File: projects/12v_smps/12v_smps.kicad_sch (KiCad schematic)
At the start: 7 parts, among them U2 TPSM82902SISR

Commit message: wip
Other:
- moved on the sheet: C1, C2, C4, R18, R19, R20, U2

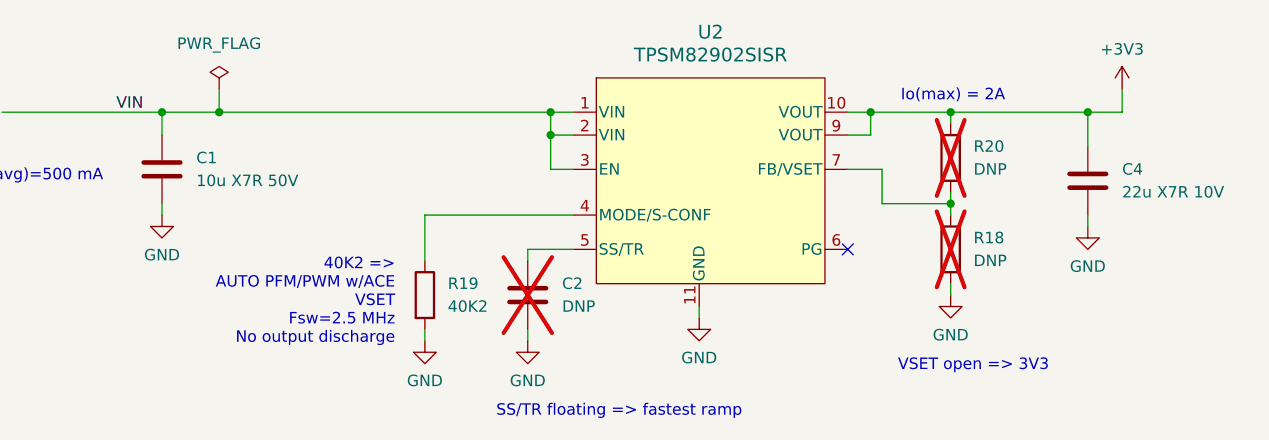
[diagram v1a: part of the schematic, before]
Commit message: 12v smps block
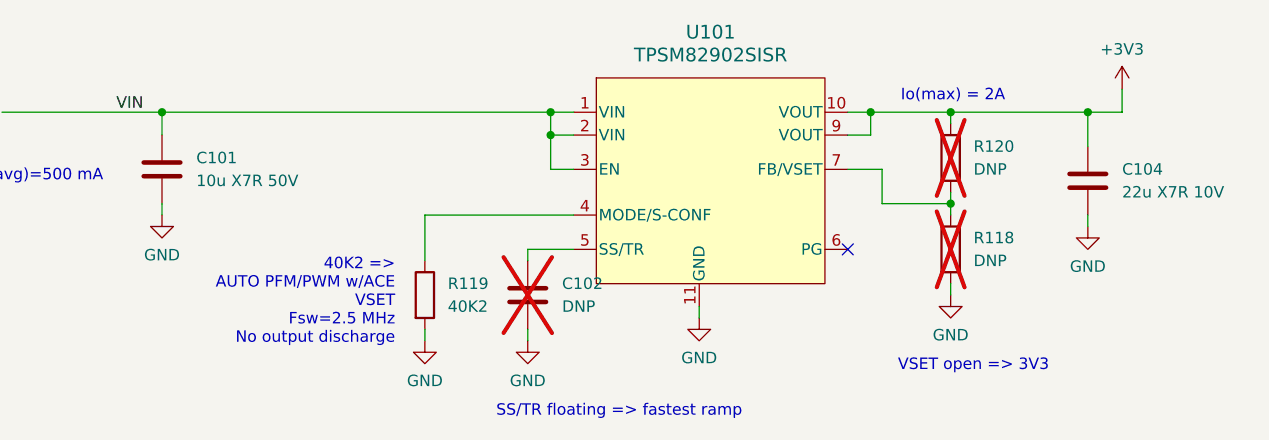
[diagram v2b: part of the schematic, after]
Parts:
- renumbered C1 to C101, C2 to C102, C4 to C104, R18 to R118, R19 to R119, R20 to R120, U2 to U101
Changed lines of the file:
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@@
-	)
-	(junction
-		(at 156.21 88.9)
-		(diameter 0)
-		(color 0 0 0 0)
 	)
 	(junction
@@
 	(wire
 		(pts
-			(xy 156.21 88.9) (xy 193.04 88.9)
+			(xy 149.86 88.9) (xy 193.04 88.9)
 		)
 		(stroke
@@
 	(wire
 		(pts
-			(xy 156.21 86.36) (xy 156.21 88.9)
-		)
-		(stroke
-			(width 0)
-			(type default)
-		)
-	)
-	(wire
-		(pts
 			(xy 149.86 99.06) (xy 149.86 100.33)
 		)
@@
 		(pts
 			(xy 256.54 86.36) (xy 256.54 88.9)
-		)
-		(stroke
-			(width 0)
-			(type default)
-		)
-	)
-	(wire
-		(pts
-			(xy 149.86 88.9) (xy 156.21 88.9)
 		)
 		(stroke
@@
 		(dnp no)
 		(fields_autoplaced yes)
-		(property "Reference" "R19"
+		(property "Reference" "R119"
 			(at 181.61 107.9499 0)
 			(effects
@@
 			(project ""
 				(path "/a5f55489-8083-4ed1-a137-3f799946f30f"
-					(reference "R19")
-					(unit 1)
-				)
-			)
-		)
-	)
-	(symbol
-		(lib_id "power:PWR_FLAG")
-		(at 156.21 86.36 0)
-		(unit 1)
-		(exclude_from_sim no)
-		(in_bom yes)
-		(on_board yes)
-		(dnp no)
-		(fields_autoplaced yes)
-		(property "Reference" "#FLG03"
-			(at 156.21 84.455 0)
-			(effects
-				(font
-					(size 1.27 1.27)
-				)
-				(hide yes)
-			)
-		)
-		(property "Value" "PWR_FLAG"
-			(at 156.21 81.28 0)
-			(effects
-				(font
-					(size 1.27 1.27)
-				)
-			)
-		)
-		(property "Footprint" ""
-			(at 156.21 86.36 0)
-			(effects
-				(font
-					(size 1.27 1.27)
-				)
-				(hide yes)
-			)
-		)
-		(property "Datasheet" "~"
-			(at 156.21 86.36 0)
-			(effects
-				(font
-					(size 1.27 1.27)
-				)
-				(hide yes)
-			)
-		)
-		(property "Description" "Special symbol for telling ERC where power comes from"
-			(at 156.21 86.36 0)
-			(effects
-				(font
-					(size 1.27 1.27)
-				)
-				(hide yes)
-			)
-		)
-		(pin "1"
-		)
-		(instances
-			(project ""
-				(path "/a5f55489-8083-4ed1-a137-3f799946f30f"
-					(reference "#FLG03")
+					(reference "R119")
 					(unit 1)
 				)
@@
 		(dnp no)
 		(fields_autoplaced yes)
-		(property "Reference" "U2"
+		(property "Reference" "U101"
 			(at 210.82 80.01 0)
 			(effects
@@
 			(project ""
 				(path "/a5f55489-8083-4ed1-a137-3f799946f30f"
-					(reference "U2")
+					(reference "U101")
 					(unit 1)
 				)
@@
 		(dnp yes)
 		(fields_autoplaced yes)
-		(property "Reference" "C2"
+		(property "Reference" "C102"
 			(at 194.31 107.9499 0)
 			(effects
@@
 			(project ""
 				(path "/a5f55489-8083-4ed1-a137-3f799946f30f"
-					(reference "C2")
+					(reference "C102")
 					(unit 1)
 				)
@@
 		(dnp yes)
 		(fields_autoplaced yes)
-		(property "Reference" "R18"
+		(property "Reference" "R118"
 			(at 240.03 102.8699 0)
 			(effects
@@
 			(project ""
 				(path "/a5f55489-8083-4ed1-a137-3f799946f30f"
-					(reference "R18")
+					(reference "R118")
 					(unit 1)
 				)
@@
 		(dnp no)
 		(fields_autoplaced yes)
-		(property "Reference" "C4"
+		(property "Reference" "C104"
 			(at 256.54 95.2499 0)
 			(effects
@@
 			(project "canob"
 				(path "/a5f55489-8083-4ed1-a137-3f799946f30f"
-					(reference "C4")
+					(reference "C104")
 					(unit 1)
 				)
@@
 		(dnp no)
 		(fields_autoplaced yes)
-		(property "Reference" "C1"
+		(property "Reference" "C101"
 			(at 153.67 93.9799 0)
 			(effects
@@
 			(project ""
 				(path "/a5f55489-8083-4ed1-a137-3f799946f30f"
-					(reference "C1")
+					(reference "C101")
 					(unit 1)
 				)
@@
 		(dnp yes)
 		(fields_autoplaced yes)
-		(property "Reference" "R20"
+		(property "Reference" "R120"
 			(at 240.03 92.7099 0)
 			(effects
@@
 			(project "canob"
 				(path "/a5f55489-8083-4ed1-a137-3f799946f30f"
-					(reference "R20")
-					(unit 1)
-				)
+					(reference "R120")
+					(unit 1)
+				)
